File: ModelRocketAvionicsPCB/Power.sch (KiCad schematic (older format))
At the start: 10 parts

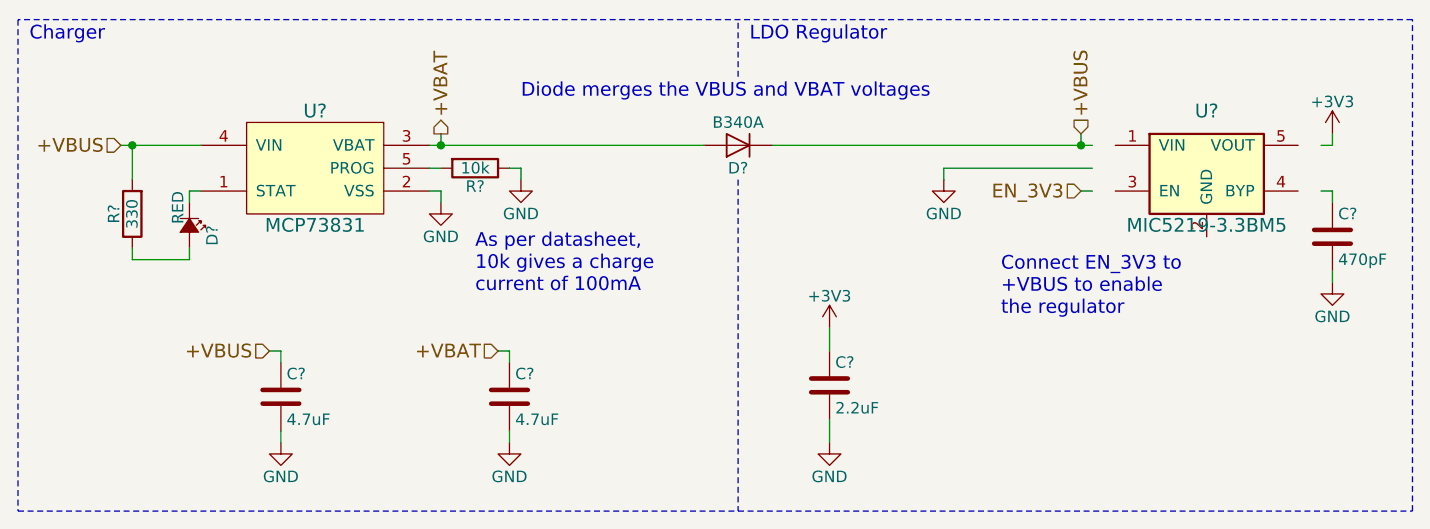
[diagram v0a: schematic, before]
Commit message: Annotated components and added 'Digi-Key Part Numbers' for most of the non-passives
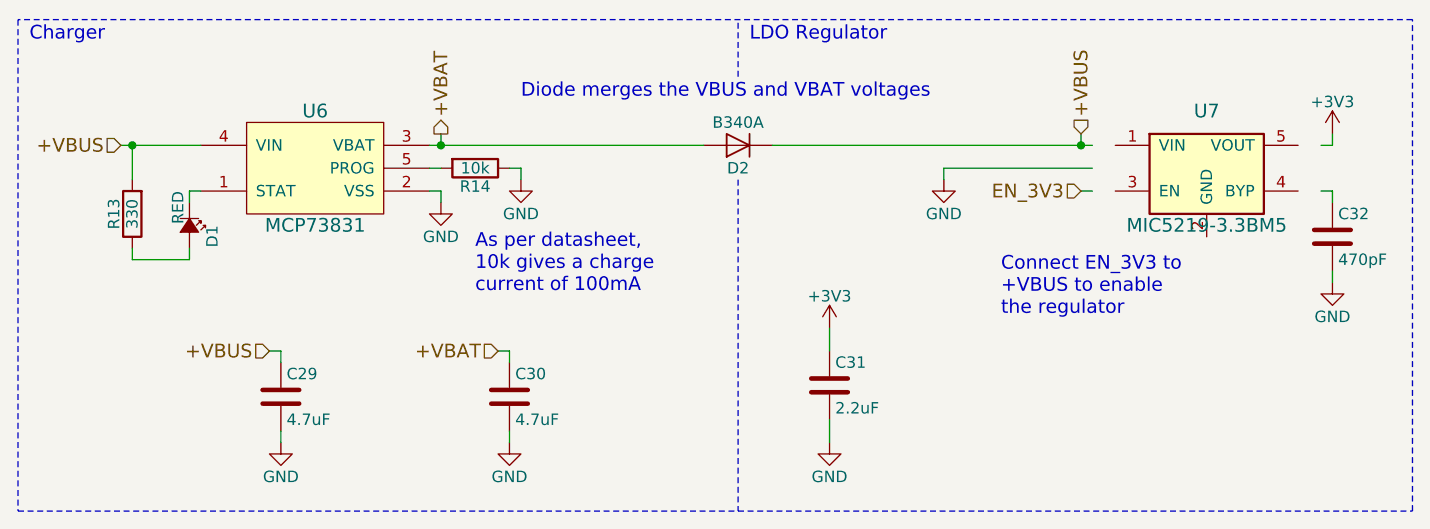
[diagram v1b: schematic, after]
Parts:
- U6: renamed from U?; Digi-Key Part Number (none) -> MCP73831T-2ACI/OTCT-ND
- U7: renamed from U?; Digi-Key Part Number (none) -> 576-1281-1-ND
- gave numbers to parts that had none: 8
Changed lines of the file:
@@
 $EndDescr
 $Comp
-L MCP73831 U?
+L MCP73831 U6
 U 1 1 5AE8FCA0
 P 3850 3250
-F 0 "U?" H 3850 3500 60  0000 C CNN
+F 0 "U6" H 3850 3500 60  0000 C CNN
 F 1 "MCP73831" H 3850 3000 60  0000 C CNN
 F 2 "" H 3850 3150 60  0001 C CNN
 F 3 "" H 3850 3150 60  0001 C CNN
+F 4 "MCP73831T-2ACI/OTCT-ND" H 3850 3250 60  0001 C CNN "Digi-Key Part Number"
 	1    3850 3250
 	1    0    0    -1
 $EndComp
 $Comp
-L MIC5219-3.3BM5 U?
+L MIC5219-3.3BM5 U7
 U 1 1 5AE8FCE7
 P 7750 3250
-F 0 "U?" H 7750 3500 60  0000 C CNN
+F 0 "U7" H 7750 3500 60  0000 C CNN
 F 1 "MIC5219-3.3BM5" H 7750 3000 60  0000 C CNN
 F 2 "" H 7750 3150 60  0001 C CNN
 F 3 "" H 7750 3150 60  0001 C CNN
+F 4 "576-1281-1-ND" H 7750 3250 60  0001 C CNN "Digi-Key Part Number"
 	1    7750 3250
 	1    0    0    -1
@@
 +VBUS
 $Comp
-L GND #PWR?
+L GND #PWR42
 U 1 1 5AE90592
 P 3700 4450
-F 0 "#PWR?" H 3700 4200 50  0001 C CNN
+F 0 "#PWR42" H 3700 4200 50  0001 C CNN
 F 1 "GND" H 3700 4300 50  0000 C CNN
 F 2 "" H 3700 4450 50  0000 C CNN
@@
 $EndComp
 $Comp
-L C C?
+L C C29
 U 1 1 5AE905AA
 P 3700 4250
-F 0 "C?" H 3725 4350 50  0000 L CNN
+F 0 "C29" H 3725 4350 50  0000 L CNN
 F 1 "4.7uF" H 3725 4150 50  0000 L CNN
 F 2 "" H 3738 4100 50  0000 C CNN
@@
 $EndComp
 $Comp
-L D D?
+L D D2
 U 1 1 5AE907ED
 P 5700 3150
-F 0 "D?" H 5700 3250 50  0000 C CNN
+F 0 "D2" H 5700 3250 50  0000 C CNN
 F 1 "B340A" H 5700 3050 50  0000 C CNN
 F 2 "" H 5700 3150 50  0000 C CNN
@@
 +VBUS
 $Comp
-L GND #PWR?
+L GND #PWR48
 U 1 1 5AE90A27
 P 6600 3300
-F 0 "#PWR?" H 6600 3050 50  0001 C CNN
+F 0 "#PWR48" H 6600 3050 50  0001 C CNN
 F 1 "GND" H 6600 3150 50  0000 C CNN
 F 2 "" H 6600 3300 50  0000 C CNN
@@
 $EndComp
 $Comp
-L R R?
+L R R14
 U 1 1 5AE90B61
 P 4550 3250
-F 0 "R?" V 4630 3250 50  0000 C CNN
+F 0 "R14" V 4630 3250 50  0000 C CNN
 F 1 "10k" V 4550 3250 50  0000 C CNN
 F 2 "" V 4480 3250 50  0000 C CNN
@@
 $EndComp
 $Comp
-L GND #PWR?
+L GND #PWR43
 U 1 1 5AE90C88
 P 4400 3400
-F 0 "#PWR?" H 4400 3150 50  0001 C CNN
+F 0 "#PWR43" H 4400 3150 50  0001 C CNN
 F 1 "GND" H 4400 3250 50  0000 C CNN
 F 2 "" H 4400 3400 50  0000 C CNN
@@
 $EndComp
 $Comp
-L GND #PWR?
+L GND #PWR45
 U 1 1 5AE90CB6
 P 4750 3300
-F 0 "#PWR?" H 4750 3050 50  0001 C CNN
+F 0 "#PWR45" H 4750 3050 50  0001 C CNN
 F 1 "GND" H 4750 3150 50  0000 C CNN
 F 2 "" H 4750 3300 50  0000 C CNN
@@
 EN_3V3
 $Comp
-L Led_Small D?
+L Led_Small D1
 U 1 1 5AE90ED9
 P 3300 3500
-F 0 "D?" H 3300 3600 50  0000 L CNN
+F 0 "D1" H 3300 3600 50  0000 L CNN
 F 1 "RED" H 3150 3450 50  0000 L CNN
 F 2 "" V 3300 3500 50  0000 C CNN
@@
 $EndComp
 $Comp
-L R R?
+L R R13
 U 1 1 5AE911EE
 P 3050 3450
-F 0 "R?" V 3130 3450 50  0000 C CNN
+F 0 "R13" V 3130 3450 50  0000 C CNN
 F 1 "330" V 3050 3450 50  0000 C CNN
 F 2 "" V 2980 3450 50  0000 C CNN
@@
 Diode merges the VBUS and VBAT voltages
 $Comp
-L C C?
+L C C32
 U 1 1 5AE91952
 P 8300 3550
-F 0 "C?" H 8325 3650 50  0000 L CNN
+F 0 "C32" H 8325 3650 50  0000 L CNN
 F 1 "470pF" H 8325 3450 50  0000 L CNN
 F 2 "" H 8338 3400 50  0000 C CNN
@@
 $EndComp
 $Comp
-L GND #PWR?
+L GND #PWR50
 U 1 1 5AE91A35
 P 8300 3750
-F 0 "#PWR?" H 8300 3500 50  0001 C CNN
+F 0 "#PWR50" H 8300 3500 50  0001 C CNN
 F 1 "GND" H 8300 3600 50  0000 C CNN
 F 2 "" H 8300 3750 50  0000 C CNN
@@
 $EndComp
 $Comp
-L +3V3 #PWR?
+L +3V3 #PWR49
 U 1 1 5AE91CF5
 P 8300 3100
-F 0 "#PWR?" H 8300 2950 50  0001 C CNN
+F 0 "#PWR49" H 8300 2950 50  0001 C CNN
 F 1 "+3V3" H 8300 3240 50  0000 C CNN
 F 2 "" H 8300 3100 50  0000 C CNN
@@
 $EndComp
 $Comp
-L +3V3 #PWR?
+L +3V3 #PWR46
 U 1 1 5AE91E05
 P 6100 3950
-F 0 "#PWR?" H 6100 3800 50  0001 C CNN
+F 0 "#PWR46" H 6100 3800 50  0001 C CNN
 F 1 "+3V3" H 6100 4090 50  0000 C CNN
 F 2 "" H 6100 3950 50  0000 C CNN
@@
 $EndComp
 $Comp
-L GND #PWR?
+L GND #PWR47
 U 1 1 5AE91E28
 P 6100 4450
-F 0 "#PWR?" H 6100 4200 50  0001 C CNN
+F 0 "#PWR47" H 6100 4200 50  0001 C CNN
 F 1 "GND" H 6100 4300 50  0000 C CNN
 F 2 "" H 6100 4450 50  0000 C CNN
@@
 $EndComp
 $Comp
-L C C?
+L C C31
 U 1 1 5AE91E4B
 P 6100 4200
-F 0 "C?" H 6125 4300 50  0000 L CNN
+F 0 "C31" H 6125 4300 50  0000 L CNN
 F 1 "2.2uF" H 6125 4100 50  0000 L CNN
 F 2 "" H 6138 4050 50  0000 C CNN
@@
 $EndComp
 $Comp
-L GND #PWR?
+L GND #PWR44
 U 1 1 5AE92741
 P 4700 4450
-F 0 "#PWR?" H 4700 4200 50  0001 C CNN
+F 0 "#PWR44" H 4700 4200 50  0001 C CNN
 F 1 "GND" H 4700 4300 50  0000 C CNN
 F 2 "" H 4700 4450 50  0000 C CNN
@@
 $EndComp
 $Comp
-L C C?
+L C C30
 U 1 1 5AE9276A
 P 4700 4250
-F 0 "C?" H 4725 4350 50  0000 L CNN
+F 0 "C30" H 4725 4350 50  0000 L CNN
 F 1 "4.7uF" H 4725 4150 50  0000 L CNN
 F 2 "" H 4738 4100 50  0000 C CNN
